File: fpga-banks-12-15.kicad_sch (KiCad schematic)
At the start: 1 part, among them U3002 XC7K160T-FFG676

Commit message: Bump revision to 1.0.0
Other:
- title: LPDDR5 Test Board -> SO-DIMM DDR5 Tester

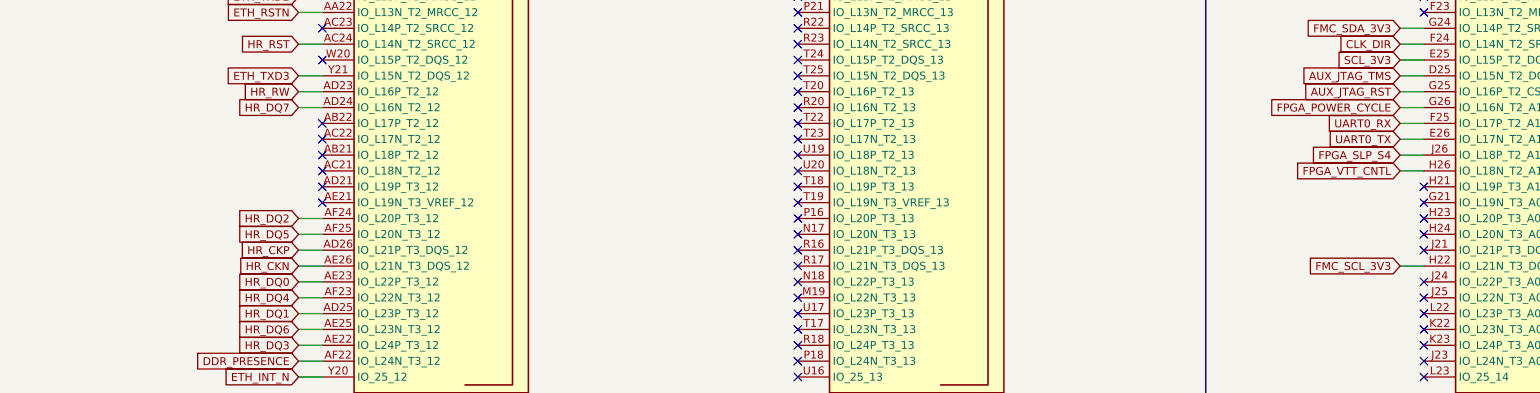
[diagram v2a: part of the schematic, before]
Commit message: Connect RFU, start improving interfaces and supply sheet, unify ESD protection
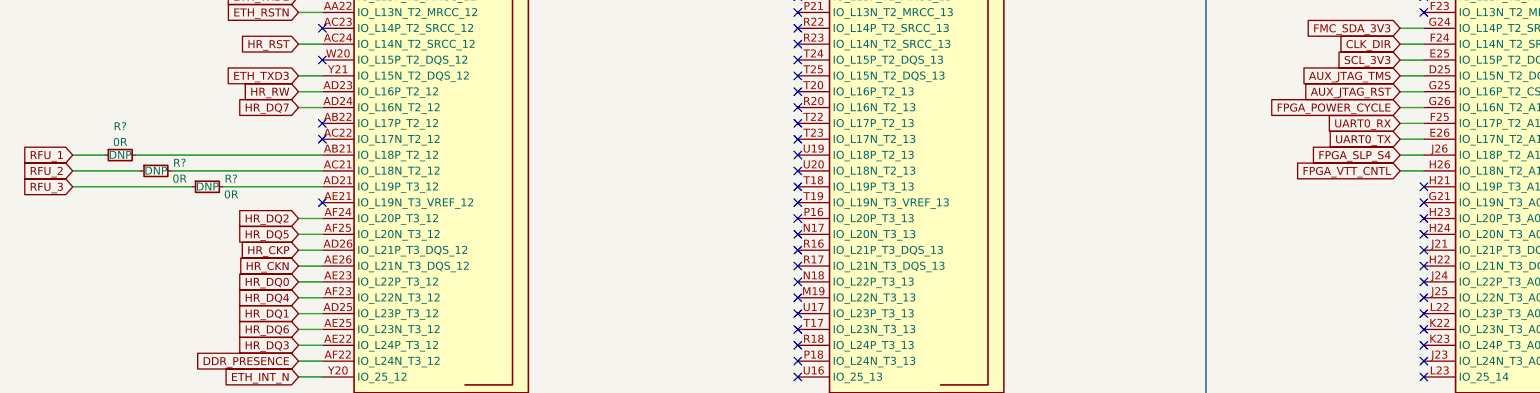
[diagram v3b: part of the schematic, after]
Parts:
- added R? (x3): R_0R_0402, antmicro-footprints:R_0402_1005Metric, symbol antmicroResistors0402:R_0R_0402
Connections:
- net at U3002.AB21 (IO_L18P_T2_12): now also R?.2
- net at U3002.AC21 (IO_L18N_T2_12): now also R?.2
- net at U3002.AD21 (IO_L19P_T3_12): now also R?.2
- net FMC_SCL_3V3: no longer names the net of U3002.H22 (IO_L21N_T3_DQS_A06_D22_14)
- new net RFU_1: R?.1
- new net RFU_2: R?.1
- new net RFU_3: R?.1
- no-connect marks 136 -> 134

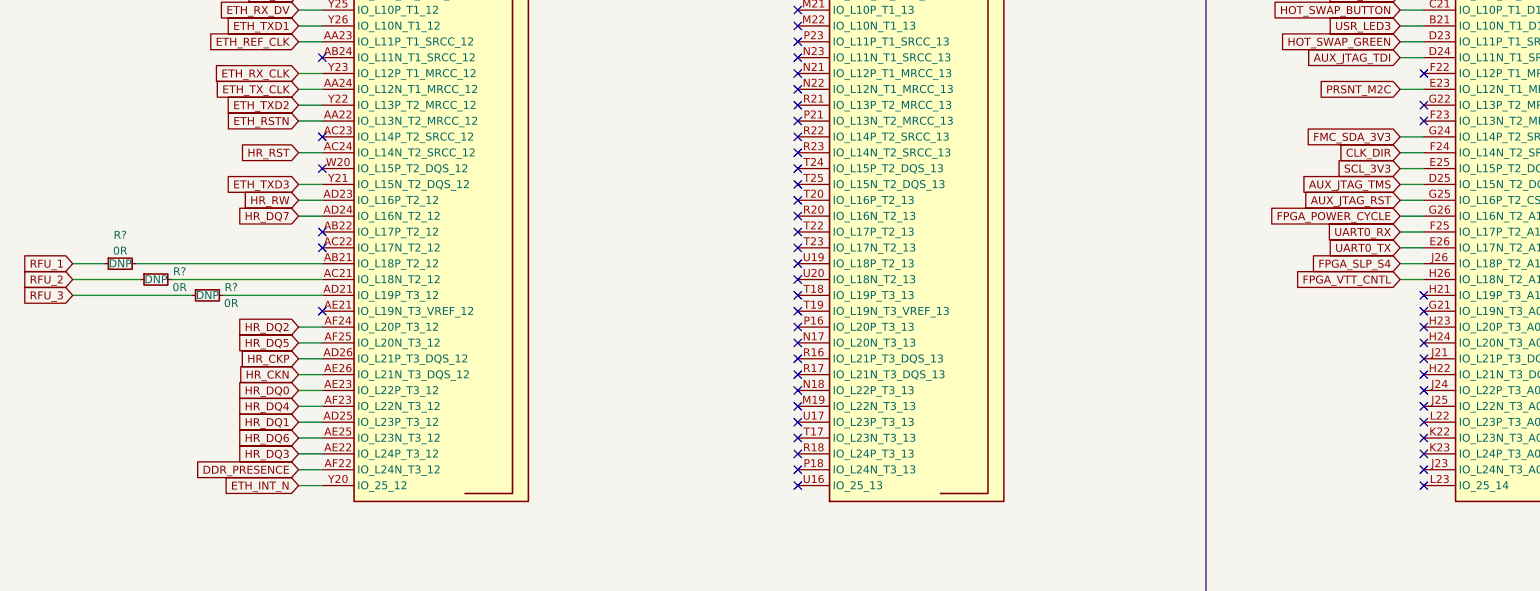
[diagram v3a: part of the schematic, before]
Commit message: Connect control and misc. signals, fix PCIe directions, rework I2C architecture, optimize DC-DC supply utilization
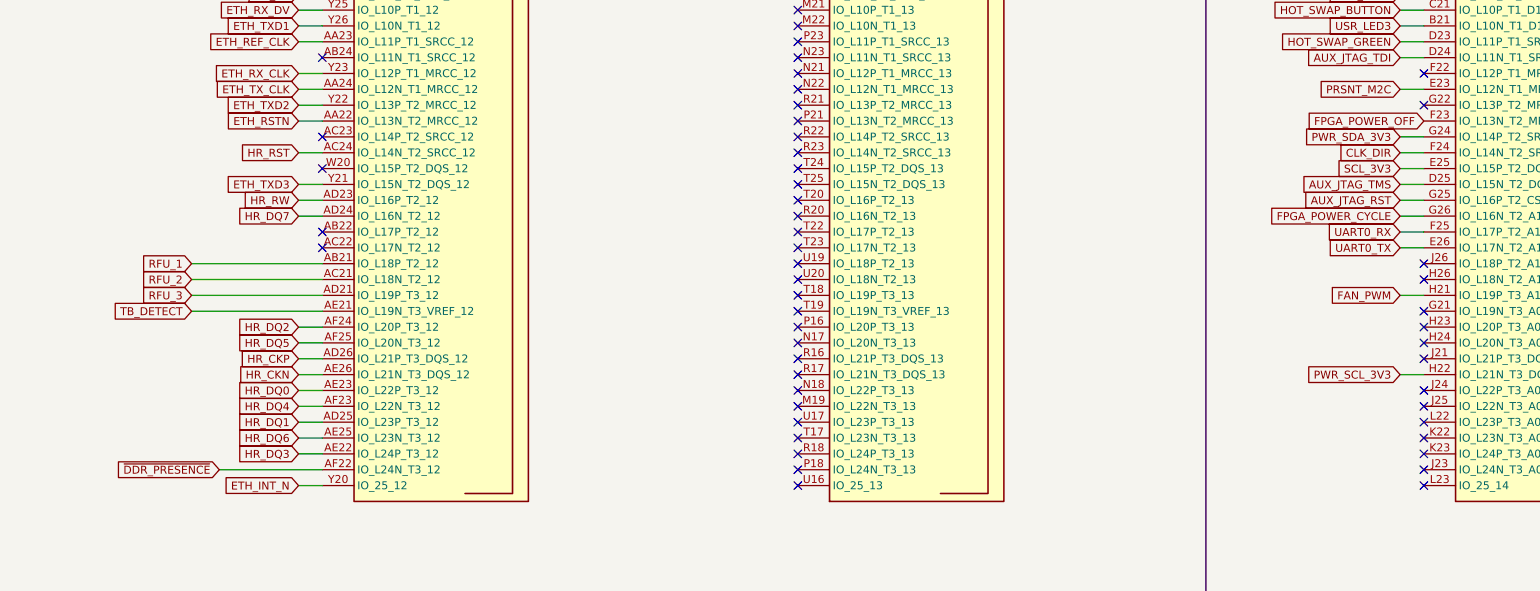
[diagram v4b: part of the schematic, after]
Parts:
- removed R? (x3): R_0R_0402, antmicro-footprints:R_0402_1005Metric, symbol antmicroResistors0402:R_0R_0402
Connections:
- net RFU_1: now also U3002.AB21 (IO_L18P_T2_12)
- net RFU_2: now also U3002.AC21 (IO_L18N_T2_12)
- net RFU_3: now also U3002.AD21 (IO_L19P_T3_12)
- net TB_DETECT: now reaches U3002.AE21 (IO_L19N_T3_VREF_12)
- net FPGA_POWER_OFF: now reaches U3002.F23 (IO_L13N_T2_MRCC_14)
- net FAN_PWM: now reaches U3002.H21 (IO_L19P_T3_A10_D26_14)
- net PWR_SCL_3V3: now reaches U3002.H22 (IO_L21N_T3_DQS_A06_D22_14)
- net DDR_PRESENCE renamed ~{DDR_PRESENCE}
- net FMC_SDA_3V3 renamed PWR_SDA_3V3
- net FPGA_SLP_S4: no longer names the net of U3002.J26 (IO_L18P_T2_A12_D28_14)
- net FPGA_VTT_CNTL: no longer names the net of U3002.H26 (IO_L18N_T2_A11_D27_14)
- no-connect marks 134 -> 132

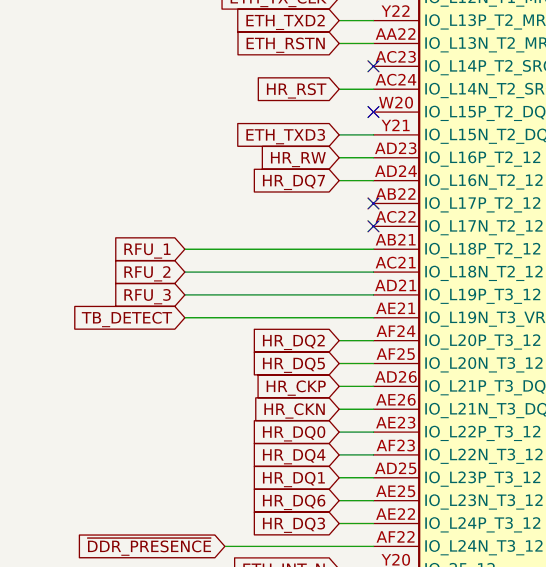
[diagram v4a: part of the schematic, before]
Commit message: Continue optimizing placement and layout of misc. circuitry
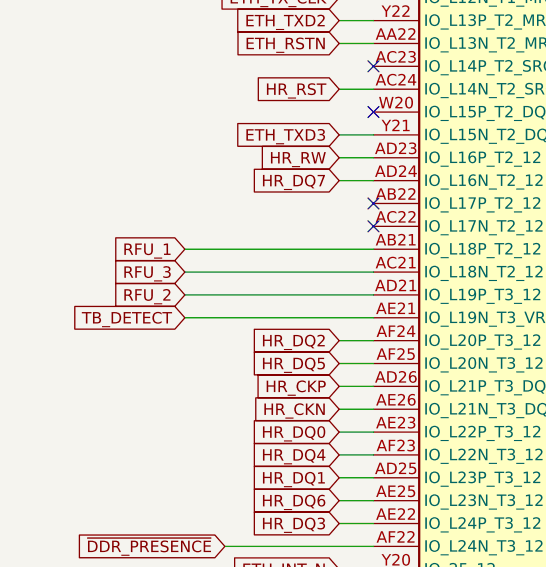
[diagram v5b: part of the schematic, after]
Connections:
- net RFU_2: now also U3002.AD21 (IO_L19P_T3_12); no longer U3002.AC21 (IO_L18N_T2_12)
- net RFU_3: now also U3002.AC21 (IO_L18N_T2_12); no longer U3002.AD21 (IO_L19P_T3_12)
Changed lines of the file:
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@@
     )
   )
-  (global_label "RFU_3" (shape input) (at 47.625 186.055 180) (fields_autoplaced)
-    (effects (font (size 1.27 1.27)) (justify right))
-    (property "Intersheet References" "${INTERSHEET_REFS}" (id 0) (at 39.4346 185.9756 0)
+  (global_label "RFU_3" (shape input) (at 47.625 183.515 180) (fields_autoplaced)
+    (effects (font (size 1.27 1.27)) (justify right))
+    (property "Intersheet References" "${INTERSHEET_REFS}" (id 0) (at 39.4346 183.4356 0)
       (effects (font (size 1.27 1.27)) (justify right) hide)
     )
@@
     )
   )
-  (global_label "RFU_2" (shape input) (at 47.625 183.515 180) (fields_autoplaced)
-    (effects (font (size 1.27 1.27)) (justify right))
-    (property "Intersheet References" "${INTERSHEET_REFS}" (id 0) (at 39.4346 183.5944 0)
-      (effects (font (size 1.27 1.27)) (justify right) hide)
-    )
+  (global_label "RFU_2" (shape input) (at 47.625 186.055 180) (fields_autoplaced)
+    (effects (font (size 1.27 1.27)) (justify right))
+    (property "Intersheet References" "${INTERSHEET_REFS}" (id 0) (at 39.4346 186.1344 0)
+      (effects (font (size 1.27 1.27)) (justify right) hide)
+    )

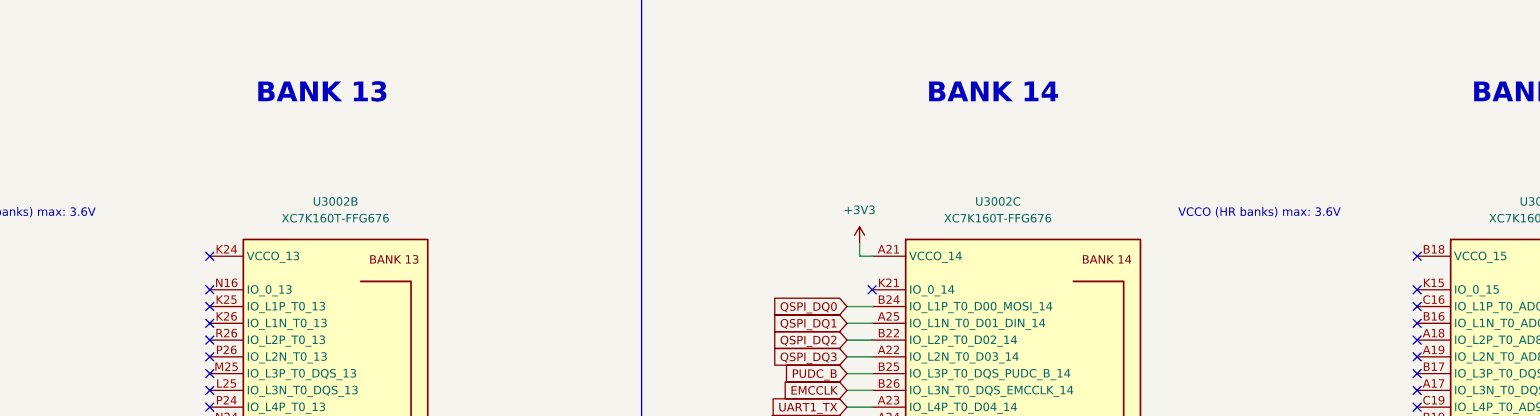
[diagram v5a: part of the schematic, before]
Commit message: Connect unused banks to 3V3 for better ESD protection, add ESD protection to SD card, add silkscreen markings
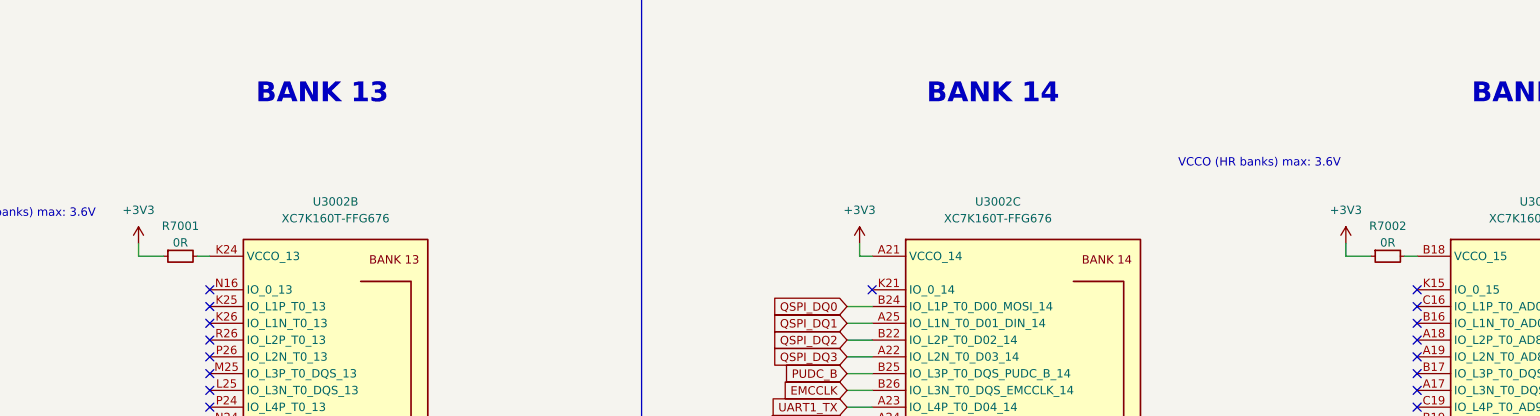
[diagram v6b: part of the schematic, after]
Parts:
- added R7001, R7002: R_0R_0402, antmicro-footprints:R_0402_1005Metric_EIA, symbol antmicroResistors0402:R_0R_0402
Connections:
- net +3V3: now also R7001.1, R7002.1
- net at U3002.K24 (VCCO_13), U3002.N25 (VCCO_13), U3002.P22 (VCCO_13)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: now also R7001.2
- net at U3002.B18 (VCCO_15), U3002.E19 (VCCO_15), U3002.F16 (VCCO_15)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: now also R7002.2
- no-connect marks 132 -> 130
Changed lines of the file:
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@@
   (no_connect (at 144.78 165.735))
   (no_connect (at 327.66 168.275))
-  (no_connect (at 144.78 86.995))
   (no_connect (at 144.78 175.895))
   (no_connect (at 144.78 135.255))
@@
   (no_connect (at 144.78 155.575))
   (no_connect (at 144.78 160.655))
-  (no_connect (at 327.66 86.995))
   (no_connect (at 327.66 104.775))
   (no_connect (at 144.78 216.535))
@@
     (stroke (width 0) (type default) (color 0 0 0 0))
   )
+  (wire (pts (xy 325.755 86.995) (xy 327.66 86.995))
+    (stroke (width 0) (type default) (color 0 0 0 0))
+  )
   (wire (pts (xy 241.3 127.635) (xy 245.11 127.635))
     (stroke (width 0) (type default) (color 0 0 0 0))
@@
     (stroke (width 0) (type default) (color 0 0 0 0))
   )
+  (wire (pts (xy 316.865 85.09) (xy 316.865 86.995))
+    (stroke (width 0) (type default) (color 0 0 0 0))
+  )
   (wire (pts (xy 64.77 158.115) (xy 68.58 158.115))
     (stroke (width 0) (type default) (color 0 0 0 0))
@@
     (stroke (width 0) (type default) (color 0 0 0 0))
   )
+  (wire (pts (xy 142.875 86.995) (xy 144.78 86.995))
+    (stroke (width 0) (type default) (color 0 0 0 0))
+  )
   (wire (pts (xy 241.3 137.795) (xy 245.11 137.795))
     (stroke (width 0) (type default) (color 0 0 0 0))
@@
     (stroke (width 0) (type default) (color 0 0 0 0))
   )
+  (wire (pts (xy 316.865 86.995) (xy 320.675 86.995))
+    (stroke (width 0) (type default) (color 0 0 0 0))
+  )
   (wire (pts (xy 241.3 198.755) (xy 245.11 198.755))
     (stroke (width 0) (type default) (color 0 0 0 0))
@@
     (stroke (width 0) (type default) (color 0 0 0 0))
   )
+  (wire (pts (xy 133.985 85.09) (xy 133.985 86.995))
+    (stroke (width 0) (type default) (color 0 0 0 0))
+  )
   (wire (pts (xy 241.3 130.175) (xy 245.11 130.175))
     (stroke (width 0) (type default) (color 0 0 0 0))
@@
     (stroke (width 0) (type default) (color 0 0 0 0))
   )
+  (wire (pts (xy 133.985 86.995) (xy 137.795 86.995))
+    (stroke (width 0) (type default) (color 0 0 0 0))
+  )
   (wire (pts (xy 64.77 153.035) (xy 68.58 153.035))
     (stroke (width 0) (type default) (color 0 0 0 0))
@@
     (effects (font (size 2.9972 2.9972) (thickness 0.5994) bold) (justify left bottom))
   )
-  (text "VCCO (HR banks) max: 3.6V" (at 291.465 81.28 0)
+  (text "VCCO (HR banks) max: 3.6V" (at 291.465 73.66 0)
     (effects (font (size 1.27 1.27)) (justify left bottom))
   )
@@
     (pin "T6")
   )
+  (symbol (lib_id "antmicroResistors0402:R_0R_0402") (at 320.675 86.995 0) (unit 1)
+    (in_bom yes) (on_board yes) (fields_autoplaced)
+    (property "Reference" "R7002" (id 0) (at 323.215 82.421 0)
+      (effects (font (size 1.27 1.27) (thickness 0.15)))
+    )
+    (property "Value" "R_0R_0402" (id 1) (at 340.995 99.695 0)
+      (effects (font (size 1.27 1.27) (thickness 0.15)) (justify left bottom) hide)
+    )
+    (property "Footprint" "antmicro-footprints:R_0402_1005Metric_EIA" (id 2) (at 340.995 102.235 0)
+      (effects (font (size 1.27 1.27) (thickness 0.15)) (justify left bottom) hide)
+    )
+    (property "Datasheet" "https://industrial.panasonic.com/cdbs/www-data/pdf/RDA0000/AOA0000C301.pdf" (id 3) (at 340.995 104.775 0)
+      (effects (font (size 1.27 1.27) (thickness 0.15)) (justify left bottom) hide)
+    )
+    (property "MPN" "ERJ2GE0R00X" (id 4) (at 340.995 107.315 0)
+      (effects (font (size 1.27 1.27) (thickness 0.15)) (justify left bottom) hide)
+    )
+    (property "Manufacturer" "Panasonic" (id 5) (at 340.995 109.855 0)
+      (effects (font (size 1.27 1.27) (thickness 0.15)) (justify left bottom) hide)
+    )
+    (property "License" "Apache-2.0" (id 6) (at 340.995 112.395 0)
+      (effects (font (size 1.27 1.27) (thickness 0.15)) (justify left bottom) hide)
+    )
+    (property "Author" "Antmicro" (id 7) (at 340.995 114.935 0)
+      (effects (font (size 1.27 1.27) (thickness 0.15)) (justify left bottom) hide)
+    )
+    (property "Val" "0R" (id 8) (at 323.215 84.9447 0)
+      (effects (font (size 1.27 1.27) (thickness 0.15)))
+    )
+    (property "Tolerance" "~" (id 9) (at 340.995 97.155 0)
+      (effects (font (size 1.27 1.27)) (justify left bottom) hide)
+    )
+    (property "Current" "1A" (id 10) (at 340.995 117.475 0)
+      (effects (font (size 1.27 1.27) (thickness 0.15)) (justify left bottom) hide)
+    )
+    (pin "1")
+    (pin "2")
+  )
   (symbol (lib_id "sodimm-ddr5-tester:XC7K160T-FFG676") (at 327.66 86.995 0) (unit 4)
     (in_bom yes) (on_board yes) (fields_autoplaced)
@@
       (effects (font (size 1.27 1.27)) hide)
     )
+    (pin "1")
+  )
+  (symbol (lib_id "antmicroResistors0402:R_0R_0402") (at 137.795 86.995 0) (unit 1)
+    (in_bom yes) (on_board yes) (fields_autoplaced)
+    (property "Reference" "R7001" (id 0) (at 140.335 82.421 0)
+      (effects (font (size 1.27 1.27) (thickness 0.15)))
+    )
+    (property "Value" "R_0R_0402" (id 1) (at 158.115 99.695 0)
+      (effects (font (size 1.27 1.27) (thickness 0.15)) (justify left bottom) hide)
+    )
+    (property "Footprint" "antmicro-footprints:R_0402_1005Metric_EIA" (id 2) (at 158.115 102.235 0)
+      (effects (font (size 1.27 1.27) (thickness 0.15)) (justify left bottom) hide)
+    )
+    (property "Datasheet" "https://industrial.panasonic.com/cdbs/www-data/pdf/RDA0000/AOA0000C301.pdf" (id 3) (at 158.115 104.775 0)
+      (effects (font (size 1.27 1.27) (thickness 0.15)) (justify left bottom) hide)
+    )
+    (property "MPN" "ERJ2GE0R00X" (id 4) (at 158.115 107.315 0)
+      (effects (font (size 1.27 1.27) (thickness 0.15)) (justify left bottom) hide)
+    )
+    (property "Manufacturer" "Panasonic" (id 5) (at 158.115 109.855 0)
+      (effects (font (size 1.27 1.27) (thickness 0.15)) (justify left bottom) hide)
+    )
+    (property "License" "Apache-2.0" (id 6) (at 158.115 112.395 0)
+      (effects (font (size 1.27 1.27) (thickness 0.15)) (justify left bottom) hide)
+    )
+    (property "Author" "Antmicro" (id 7) (at 158.115 114.935 0)
+      (effects (font (size 1.27 1.27) (thickness 0.15)) (justify left bottom) hide)
+    )
+    (property "Val" "0R" (id 8) (at 140.335 84.9447 0)
+      (effects (font (size 1.27 1.27) (thickness 0.15)))
+    )
+    (property "Tolerance" "~" (id 9) (at 158.115 97.155 0)
+      (effects (font (size 1.27 1.27)) (justify left bottom) hide)
+    )
+    (property "Current" "1A" (id 10) (at 158.115 117.475 0)
+      (effects (font (size 1.27 1.27) (thickness 0.15)) (justify left bottom) hide)
+    )
+    (pin "1")
+    (pin "2")
+  )
+  (symbol (lib_id "sodimm-ddr5-tester:+3V3") (at 133.985 85.09 0) (unit 1)
+    (in_bom yes) (on_board yes) (fields_autoplaced)
+    (property "Reference" "#PWR0290" (id 0) (at 133.985 88.9 0)
+      (effects (font (size 1.27 1.27)) hide)
+    )
+    (property "Value" "+3V3" (id 1) (at 133.985 80.01 0))
+    (property "Footprint" "" (id 2) (at 133.985 85.09 0)
+      (effects (font (size 1.27 1.27)) hide)
+    )
+    (property "Datasheet" "" (id 3) (at 133.985 85.09 0)
+      (effects (font (size 1.27 1.27)) hide)
+    )
+    (pin "1")
+  )
+  (symbol (lib_id "sodimm-ddr5-tester:+3V3") (at 316.865 85.09 0) (unit 1)
+    (in_bom yes) (on_board yes) (fields_autoplaced)
+    (property "Reference" "#PWR0289" (id 0) (at 316.865 88.9 0)
+      (effects (font (size 1.27 1.27)) hide)
+    )
+    (property "Value" "+3V3" (id 1) (at 316.865 80.01 0))
+    (property "Footprint" "" (id 2) (at 316.865 85.09 0)
+      (effects (font (size 1.27 1.27)) hide)
+    )
+    (property "Datasheet" "" (id 3) (at 316.865 85.09 0)
+      (effects (font (size 1.27 1.27)) hide)
+    )
